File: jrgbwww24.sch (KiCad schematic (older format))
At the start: 20 parts

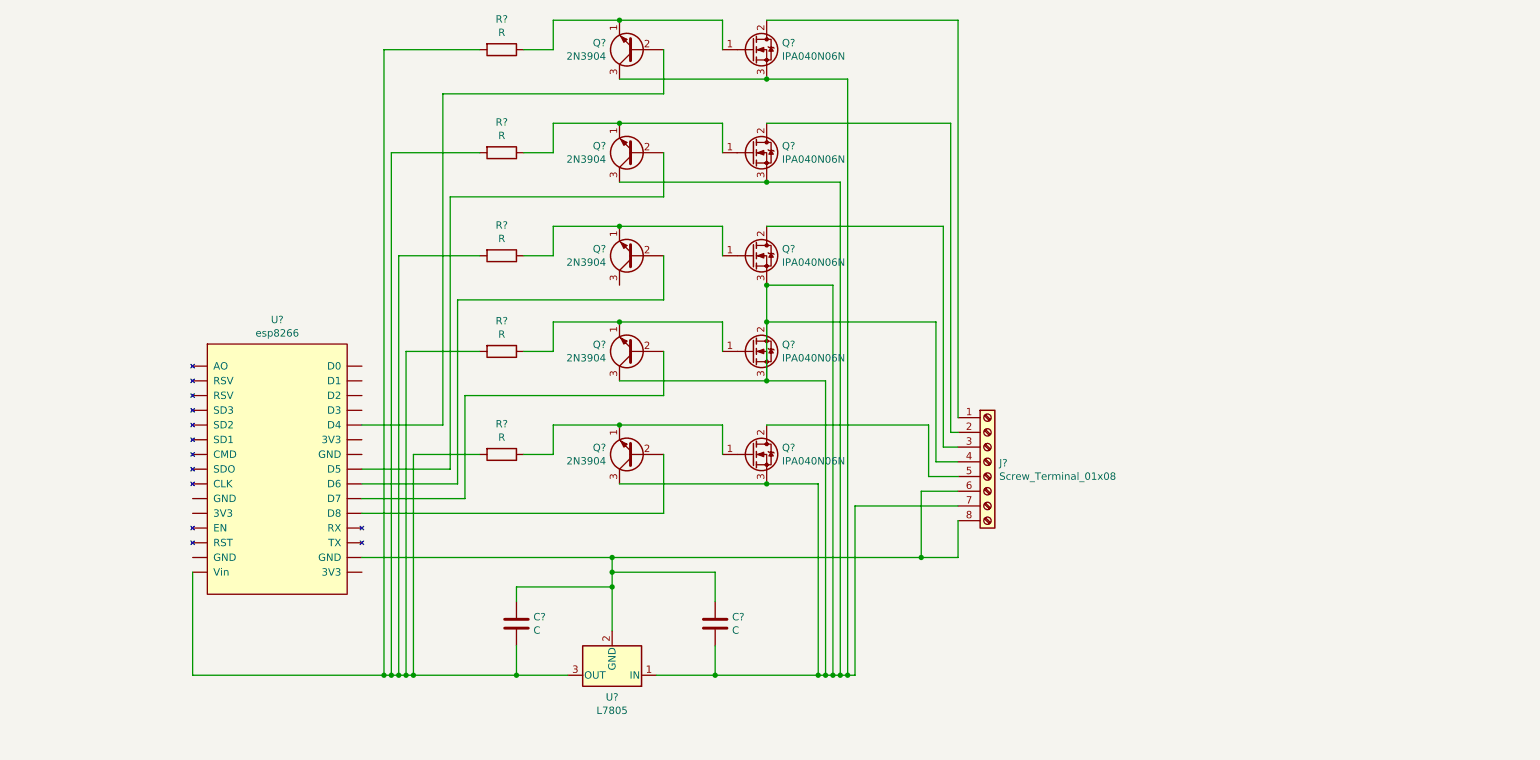
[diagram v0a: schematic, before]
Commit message: labeled connections
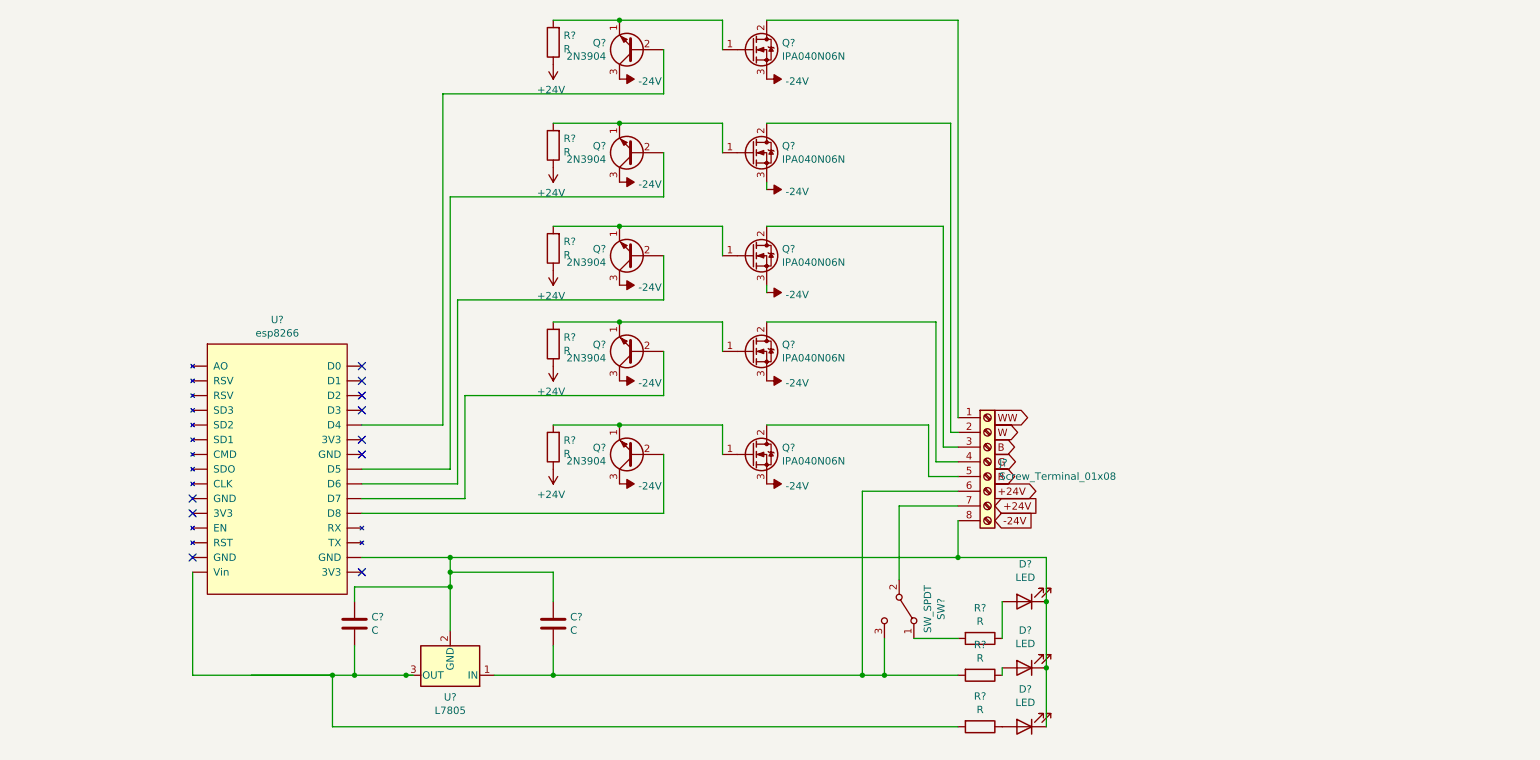
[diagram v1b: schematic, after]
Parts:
- added D? (x3): LED, symbol Device:LED
- added R? (x3): R, symbol Device:R
- added SW?: SW_SPDT, symbol Switch:SW_SPDT
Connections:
- net at U?.~ (Vin): now also Q?.2 (B)
- net at C?.1, C?.2, J?.8 (GNG)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: now also D?.1 (K), D?.1 (K), D?.1 (K); no longer J?.6 (24V)
- net at Q?.1 (E), Q?.1 (G): now also R?.2; no longer R?.1 (x5)
- net -24V: now reaches Q?.3 (C)
- net -24V: now also Q?.3 (C), Q?.3 (C), Q?.3 (C), Q?.3 (C), Q?.3 (S), Q?.3 (S), Q?.3 (S), Q?.3 (S), Q?.3 (S), Q?.5 (S), Q?.5 (S), Q?.5 (S), Q?.5 (S), Q?.5 (S), Q?.6 (S), Q?.6 (S), Q?.6 (S), Q?.6 (S), Q?.6 (S), Q?.7 (S), Q?.7 (S), Q?.7 (S), Q?.7 (S), Q?.7 (S)
- new net: C?.1, R?.2, U?.3 (OUT), U?.~ (Vin)
- new net: C?.2, J?.6 (24V), R?.2, SW?.3 (C), U?.1 (IN)
- new net: J?.4 (G), Q?.2 (D)
- new net: J?.7 (24V), SW?.2 (B)
- new net: R?.2, SW?.1 (A)
- new net: D?.2 (A), R?.1 (x3)
- new net +24V: R?.1, R?.1, R?.1, R?.1, R?.1
- no-connect marks 0 -> 10
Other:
- moved on the sheet: C?, R?, U?

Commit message: schmea refactor
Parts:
- removed D? (x2): LED, symbol Device:LED
- removed J?: Screw_Terminal_01x08, symbol library:Screw_Terminal_01x08
- removed Q? (x4): 2N3904, Package_TO_SOT_THT:TO-92_Inline, symbol Transistor_BJT:2N3904
- removed Q? (x4): IPA040N06N, Package_TO_SOT_SMD:TO-263-6, symbol library:IPA040N06N
- removed R? (x6): R, symbol Device:R
- added D?: YELLOW - 5V, symbol Device:LED
- added D?: BLUE - 24V, symbol Device:LED
- added J?: Screw_Terminal_01x06, symbol Connector:Screw_Terminal_01x06
- added J?: Srew_terminal, symbol Connector:Screw_Terminal_01x02
- added Q? (x4): 2N3904, Package_TO_SOT_THT:TO-92_Inline, symbol Transistor_BJT:2N3904
- added Q? (x4): IPA040N06N, Package_TO_SOT_SMD:TO-263-6, symbol library:IPA040N06N
- added R? (x4): 10K, symbol Device:R
- added R?: 125, symbol Device:R
- added R?: 1.05K, symbol Device:R
- C?: value C -> 0.1u
- C?: value C -> 0.33u
- D?: value LED -> RED - ALWAY ON
- R?: value R -> 10K
- R?: value R -> 1.1K
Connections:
- net +24V: now also R?.2, SW?.2 (B), J?.1 (Pin_1), J?.2 (Pin_2), R?.1, R?.1, R?.1, R?.1, R?.2
- net WW_SIGNAL: now reaches U?.~ (Vin)
- net WW_SIGNAL: now also Q?.2 (B)
- net R_SIGNAL: now reaches Q?.2 (B), U?.~ (Vin)
- net R_GND: now reaches Q?.2 (D)
- net R_GND: now also J?.2 (Pin_2)
- net at Q?.1 (G), R?.2: now also Q?.3 (C); no longer Q?.1 (E)
- net at SW?.1 (A): now also C?.2, U?.1 (IN); no longer R?.2
- net -24V renamed Earth
- net Earth: now also C?.1, C?.2, D?.1 (K), Q?.1 (E), U?.2 (GND), U?.~ (Vin), D?.1 (K), D?.1 (K), J?.1 (Pin_1), Q?.1 (E), Q?.1 (E), Q?.1 (E), Q?.1 (E), Q?.3 (S), Q?.3 (S), Q?.3 (S), Q?.3 (S), Q?.5 (S), Q?.5 (S), Q?.5 (S), Q?.5 (S), Q?.6 (S), Q?.6 (S), Q?.6 (S), Q?.6 (S), Q?.7 (S), Q?.7 (S), Q?.7 (S), Q?.7 (S); no longer Q?.3 (C)
- new net: Q?.1 (G), Q?.3 (C), R?.2 (x4)
- new net: D?.2 (A), R?.1 (x2)
- new net +5V: C?.1, R?.2, U?.3 (OUT), U?.~ (Vin)
- new net B_GND: J?.4 (Pin_4), Q?.2 (D)
- new net B_SIGNAL: Q?.2 (B), U?.~ (Vin)
- new net CW_GND: J?.5 (Pin_5), Q?.2 (D)
- new net CW_SIGNAL: Q?.2 (B), U?.~ (Vin)
- new net G_GND: J?.3 (Pin_3), Q?.2 (D)
- new net G_SIGNAL: Q?.2 (B), U?.~ (Vin)
- new net WW_GND: J?.6 (Pin_6), Q?.2 (D)
- now unconnected: SW?.3 (C)
- no-connect marks 10 -> 8
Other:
- moved on the sheet: C?, D?, Q?, R?, SW?, U?

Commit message: annotations
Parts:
- R1: renamed from R?; footprint (none) -> Resistor_THT:R_Box_L8.4mm_W2.5mm_P5.08mm
- gave numbers to parts that had none: 27
